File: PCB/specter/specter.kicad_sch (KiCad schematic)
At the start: 132 parts, among them J1 USB_C_Receptacle_USB2.0_16P, J2 Micro_SD_Card_Det2, J22 SM04B-SRSS-TB_LF__SN_, J23 Conn_01x01, J24 SM04B-SRSS-TB_LF__SN_, J25 SM04B-SRSS-TB_LF__SN_, J26 SM04B-SRSS-TB_LF__SN_, J27 SM06B-SRSS-TB_LF__SN_, J28 SM06B-SRSS-TB_LF__SN_, J29 SM06B-SRSS-TB_LF__SN_, J3 Bus_M.2_Socket_M, J30 SM06B-SRSS-TB_LF__SN_, J4 Conn_01x22_Socket, J5 Conn_01x22_Socket, J6 Conn_02x01, J7 Conn_01x03, J8 Conn_01x01, J9 Conn_02x01, M1 M.2 Screw, M2 M.2 Solder Nut, M3 M.2 Solder Nut, U1 FT232RL, U10 ASEK-32.768KHZ-L-R-T, U2 FT232RL, U3 RT9742GGJ5, U4 MagJack-A70-112-331N126, U5 TPD4EUSB30, U6 TPD4EUSB30, U7 74LVC1G07_copy, U8 AP2553W6, U9 AP3441SHE-7B

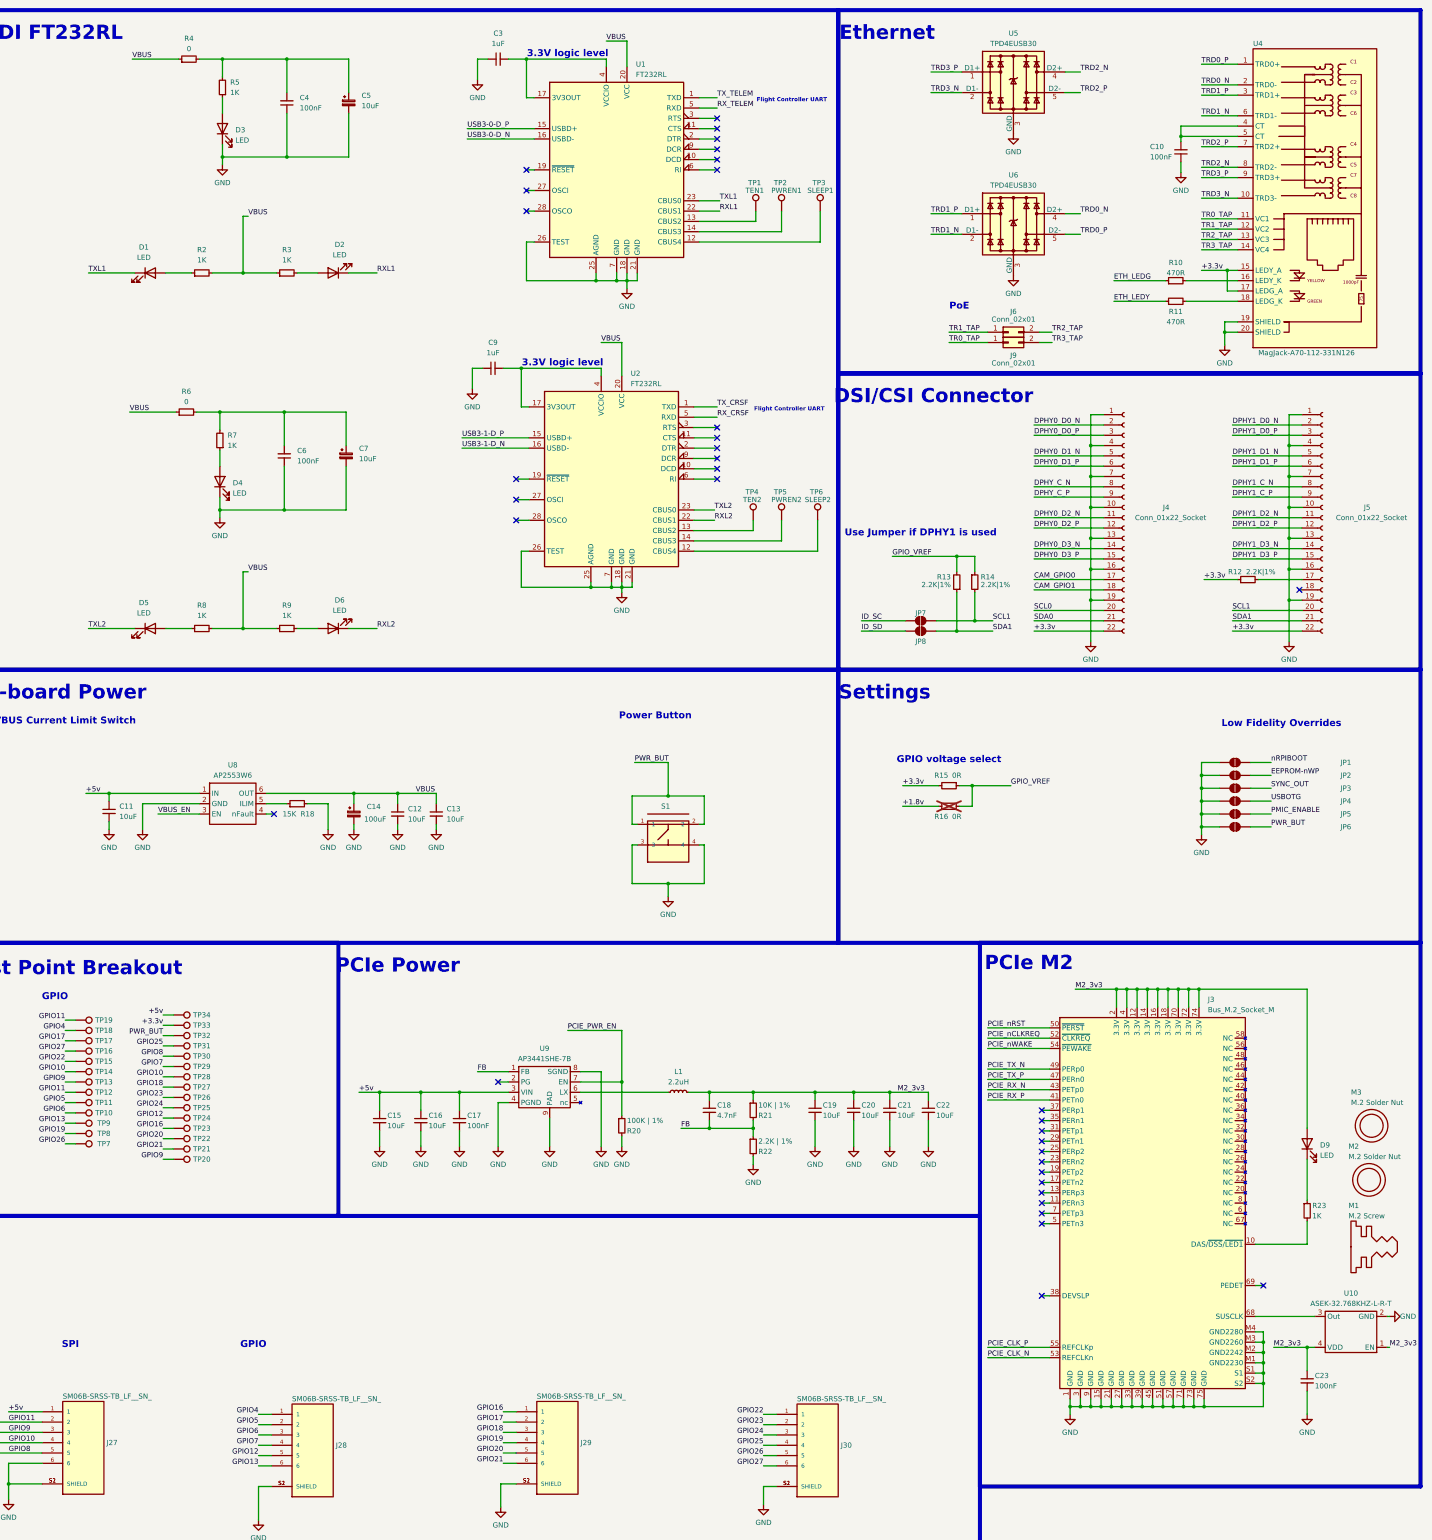
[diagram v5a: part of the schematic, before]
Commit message: GPIO wired
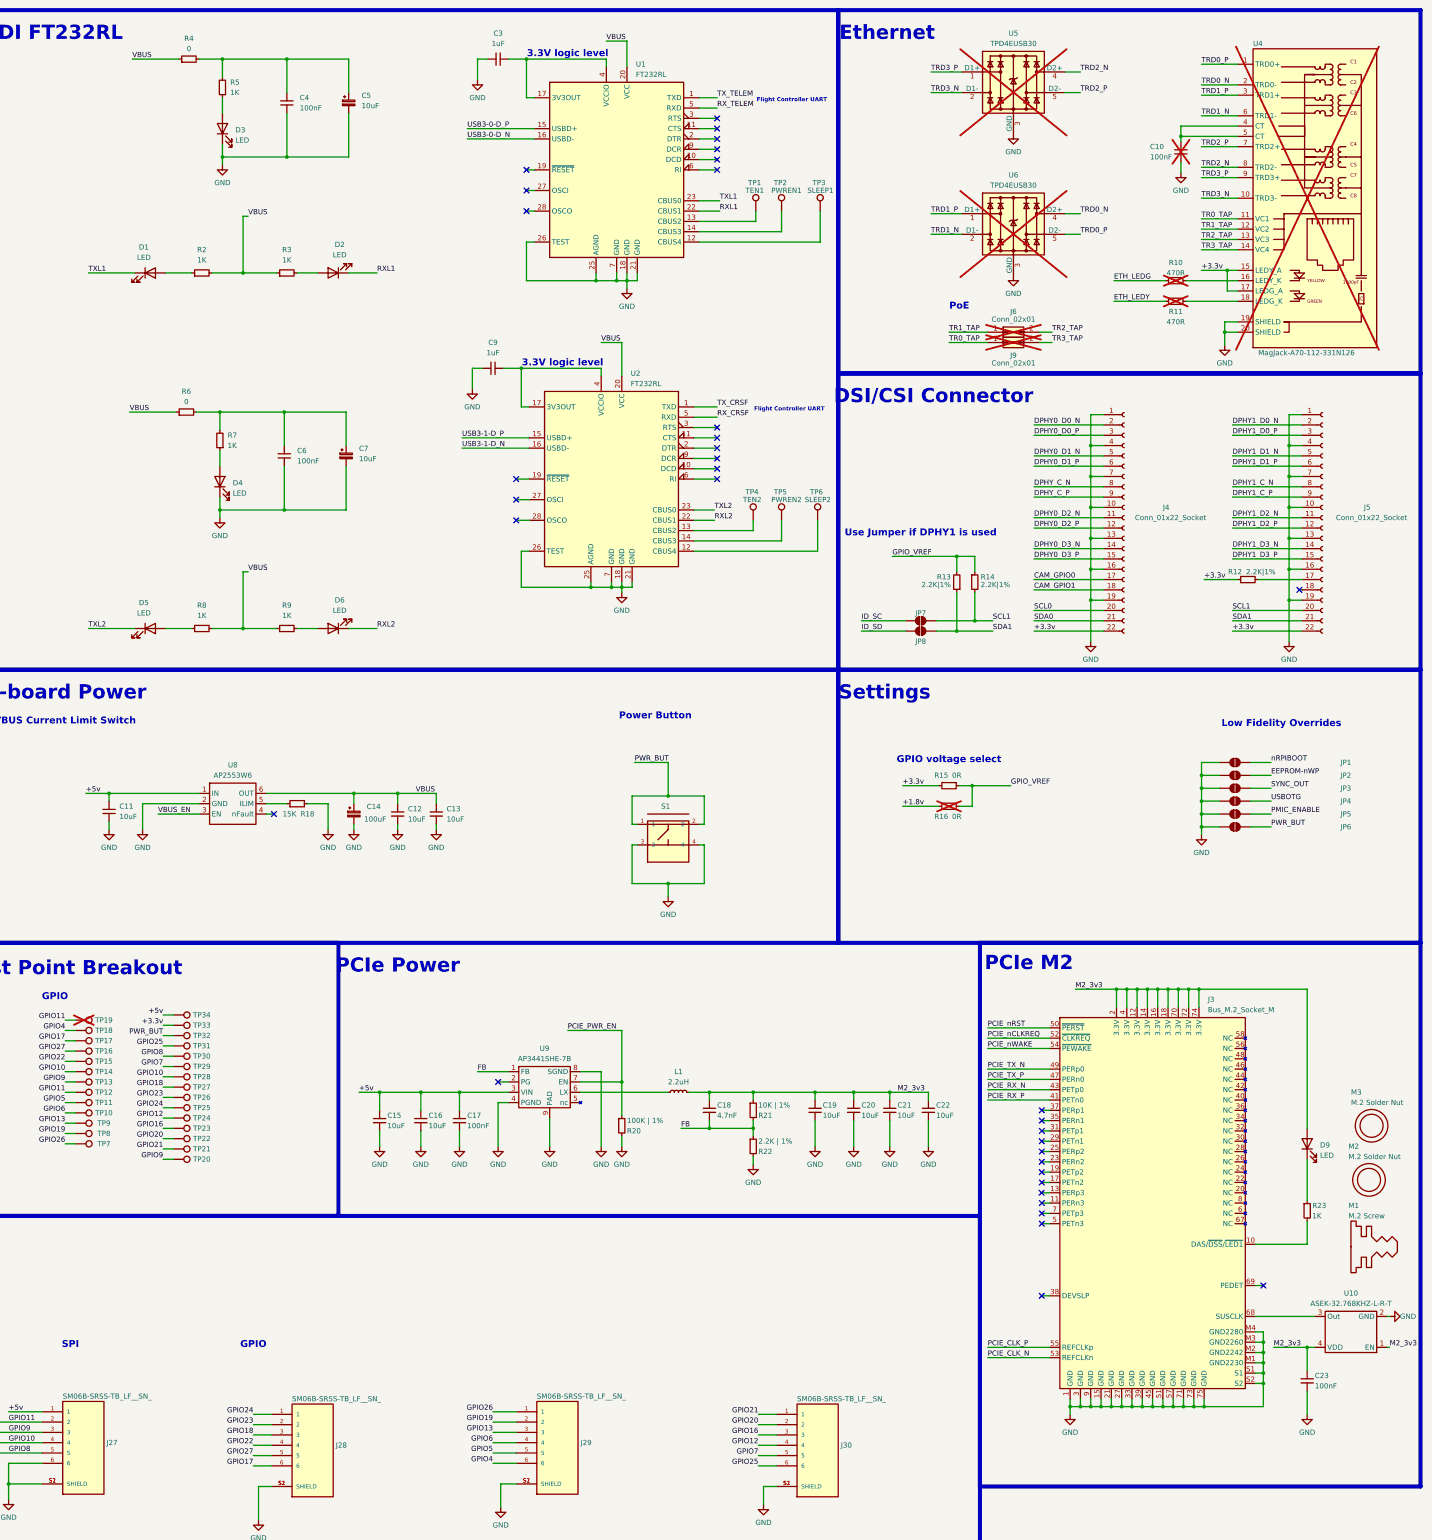
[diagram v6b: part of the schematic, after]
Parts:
- C10, J6, J9, R10, R11, TP19, U4, U5, U6: now not fitted
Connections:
- net GPIO12: now also J30.4; no longer J28.5
- net GPIO13: now also J29.3; no longer J28.6
- net GPIO16: now also J30.3; no longer J29.1
- net GPIO17: now also J28.6; no longer J29.2
- net GPIO18: now also J28.3; no longer J29.3
- net GPIO19: now also J29.2; no longer J29.4
- net GPIO20: now also J30.2; no longer J29.5
- net GPIO21: now also J30.1; no longer J29.6
- net GPIO22: now also J28.4; no longer J30.1
- net GPIO23: now also J28.2; no longer J30.2
- net GPIO24: now also J28.1; no longer J30.3
- net GPIO25: now also J30.6; no longer J30.4
- net GPIO26: now also J29.1; no longer J30.5
- net GPIO27: now also J28.5; no longer J30.6
- net GPIO4: now also J29.6; no longer J28.1
- net GPIO5: now also J29.5; no longer J28.2
- net GPIO6: now also J29.4; no longer J28.3
- net GPIO7: now also J30.5; no longer J28.4

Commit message: refined PCB
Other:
- note added: "Checked"
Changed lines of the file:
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@@
 		)
 	)
+	(text "Checked\n"
+		(exclude_from_sim no)
+		(at 445.77 110.49 0)
+		(effects
+			(font
+				(face "Avenir Next")
+				(size 1.7 1.7)
+				(bold yes)
+				(color 0 255 0 1)
+			)
+		)
+	)
 	(text "3.3V logic level"
 		(exclude_from_sim no)
@@
 		)
 	)
+	(text "Checked\n"
+		(exclude_from_sim no)
+		(at 445.77 20.828 0)
+		(effects
+			(font
+				(face "Avenir Next")
+				(size 1.7 1.7)
+				(bold yes)
+				(color 0 255 0 1)
+			)
+		)
+	)
 	(text "GPIO"
 		(exclude_from_sim no)
@@
 		)
 	)
+	(text "Checked\n"
+		(exclude_from_sim no)
+		(at 233.172 21.082 0)
+		(effects
+			(font
+				(face "Avenir Next")
+				(size 1.7 1.7)
+				(bold yes)
+				(color 0 255 0 1)
+			)
+		)
+	)
 	(text "Power Button"
 		(exclude_from_sim no)
@@
 		)
 	)
+	(text "Checked\n"
+		(exclude_from_sim no)
+		(at 18.796 20.32 0)
+		(effects
+			(font
+				(face "Avenir Next")
+				(size 1.7 1.7)
+				(bold yes)
+				(color 0 255 0 1)
+			)
+		)
+	)
 	(text "Power In"
 		(exclude_from_sim no)
@@
 		(at 459.105 165.1 0)
 		(unit 1)
-		(exclude_from_sim yes)
+		(exclude_from_sim no)
 		(in_bom no)
 		(on_board yes)
@@
 		(dnp no)
 		(property "Reference" "J4"
-			(at 518.795 134.62 0)
+			(at 497.713 105.918 0)
 			(effects
 				(font
@@
 		)
 		(property "Value" "Conn_01x22_Socket"
-			(at 520.7 137.16 0)
+			(at 499.618 108.458 0)
 			(effects
 				(font
@@
 		(at 459.105 162.56 0)
 		(unit 1)
-		(exclude_from_sim yes)
+		(exclude_from_sim no)
 		(in_bom no)
 		(on_board yes)
@@
 		(dnp no)
 		(property "Reference" "J5"
-			(at 568.325 134.62 0)
+			(at 547.243 105.918 0)
 			(effects
 				(font
@@
 		)
 		(property "Value" "Conn_01x22_Socket"
-			(at 570.23 137.16 0)
+			(at 549.148 108.458 0)
 			(effects
 				(font
